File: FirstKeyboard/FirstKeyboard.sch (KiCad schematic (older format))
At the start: 2 parts

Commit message: A little more done
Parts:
- added C? (x2): 22pF, symbol Device:C_Small
- added C?: 100n, symbol Device:C_Small
- added C?: 1uF, symbol Device:C_Small
- added R? (x2): 10k, symbol Device:R_Small
- added SW?: SW_Push, symbol Switch:SW_Push
- added Y?: 16MHz, symbol Device:Crystal_Small
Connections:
- net +5V: now also R?.2
- net GND: now also C?.1, C?.1, C?.2, R?.1, SW?.1
- net RST: now reaches U?.13 (~RESET)
- net RST: now also C?.2, R?.1, SW?.2
- net at U?.16 (XTAL2): now also C?.2, Y?.1
- net at U?.17 (XTAL1): now also C?.1, Y?.2
- net at U?.33 (~HWB~/PE2): now also R?.2
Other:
- moved on the sheet: C?, U?

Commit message: Morning Updates Dec9
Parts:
- removed C?: 1uF, symbol Device:C_Small
- added C? (x2): 100n, symbol Device:C_Small
- added C?: 1uF, symbol Device:C_Small
- added C?: 10uF, symbol Device:C_Small
- added J?: USB_B_Mini, symbol Connector:USB_B_Mini
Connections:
- net +5V: now also C?.1, C?.1, C?.1, C?.1
- net GND: now also C?.2, C?.2, C?.2, C?.2
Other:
- moved on the sheet: C?, R?, SW?, U?, Y?

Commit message: added gitignore and other files
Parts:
- added D1, D2, D3, D4: D_Small, symbol Device:D_Small
- added R2, R3: 22R, symbol Device:R_Small
- added SW1, SW2, SW3, SW4: MXSwitch, symbol acheronSymbols:MXSwitch
- gave numbers to parts that had none: 14
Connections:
- net +5V: now also J1.1 (VBUS)
- net GND: now also J1.5 (GND)
- net at U1.3 (D-): now also R3.2
- net at U1.4 (D+): now also R2.1
- net at J1.2 (D-): now also R3.1
- net at J1.3 (D+): now also R2.2
- new net: D1.2 (A), SW1.2 (Row)
- new net: D3.2 (A), SW3.2 (Row)
- new net: D4.2 (A), SW4.2 (Row)
- new net: D2.2 (A), SW2.2 (Row)
- new net Col1: D1.1 (K), D3.1 (K)
- new net Col2: D2.1 (K), D4.1 (K)
- new net Row1: SW1.1 (Col), SW2.1 (Col)
- new net Row2: SW3.1 (Col), SW4.1 (Col)
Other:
- moved on the sheet: C1, C2, C3, C4, C5, C6, C7, C8, J1, R1, R4, SWP1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

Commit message: Last update of the day
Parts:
- C1, C2, C3, C4, C5, C6, C7, C8: footprint (none) -> Capacitor_SMD:C_0805_2012Metric_Pad1.15x1.40mm_HandSolder
- D1, D2, D3, D4: footprint (none) -> Diode_SMD:D_SOD-123
- J1: footprint (none) -> acheron_Connectors:USB_MiniB_XM7D-0512
- R1, R2, R3, R4: footprint (none) -> Resistor_SMD:R_1206_3216Metric_Pad1.42x1.75mm_HandSolder
- SW1, SW2, SW3, SW4: footprint (none) -> acheron_MX:MX100
- SWP1: footprint (none) -> acheron_Hardware:smdPushBtn
- Y1: footprint (none) -> Crystal:Crystal_SMD_5032-2Pin_5.0x3.2mm_HandSoldering
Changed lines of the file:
@@
 F 0 "SW1" H 7000 3000 50  0000 L CNN
 F 1 "MXSwitch" H 6950 2925 39  0000 L CNN
-F 2 "" H 7075 2925 50  0001 C CNN
+F 2 "acheron_MX:MX100" H 7075 2925 50  0001 C CNN
 F 3 "" H 7075 2925 50  0001 C CNN
 	1    7075 2925
@@
 F 0 "D1" V 7029 2543 50  0000 L CNN
 F 1 "D_Small" V 7120 2543 50  0000 L CNN
-F 2 "" V 7075 2475 50  0001 C CNN
+F 2 "Diode_SMD:D_SOD-123" V 7075 2475 50  0001 C CNN
 F 3 "~" V 7075 2475 50  0001 C CNN
 	1    7075 2475
@@
 F 0 "SW3" H 7925 3000 50  0000 L CNN
 F 1 "MXSwitch" H 7875 2925 39  0000 L CNN
-F 2 "" H 8000 2925 50  0001 C CNN
+F 2 "acheron_MX:MX100" H 8000 2925 50  0001 C CNN
 F 3 "" H 8000 2925 50  0001 C CNN
 	1    8000 2925
@@
 F 0 "D3" V 7954 2543 50  0000 L CNN
 F 1 "D_Small" V 8045 2543 50  0000 L CNN
-F 2 "" V 8000 2475 50  0001 C CNN
+F 2 "Diode_SMD:D_SOD-123" V 8000 2475 50  0001 C CNN
 F 3 "~" V 8000 2475 50  0001 C CNN
 	1    8000 2475
@@
 F 0 "SW4" H 7925 4275 50  0000 L CNN
 F 1 "MXSwitch" H 7875 4200 39  0000 L CNN
-F 2 "" H 8000 4200 50  0001 C CNN
+F 2 "acheron_MX:MX100" H 8000 4200 50  0001 C CNN
 F 3 "" H 8000 4200 50  0001 C CNN
 	1    8000 4200
@@
 F 0 "D4" V 7954 3818 50  0000 L CNN
 F 1 "D_Small" V 8045 3818 50  0000 L CNN
-F 2 "" V 8000 3750 50  0001 C CNN
+F 2 "Diode_SMD:D_SOD-123" V 8000 3750 50  0001 C CNN
 F 3 "~" V 8000 3750 50  0001 C CNN
 	1    8000 3750
@@
 F 0 "SW2" H 7000 4275 50  0000 L CNN
 F 1 "MXSwitch" H 6950 4200 39  0000 L CNN
-F 2 "" H 7075 4200 50  0001 C CNN
+F 2 "acheron_MX:MX100" H 7075 4200 50  0001 C CNN
 F 3 "" H 7075 4200 50  0001 C CNN
 	1    7075 4200
@@
 F 0 "D2" V 7029 3818 50  0000 L CNN
 F 1 "D_Small" V 7120 3818 50  0000 L CNN
-F 2 "" V 7075 3750 50  0001 C CNN
+F 2 "Diode_SMD:D_SOD-123" V 7075 3750 50  0001 C CNN
 F 3 "~" V 7075 3750 50  0001 C CNN
 	1    7075 3750
@@
 F 0 "R3" V 2604 5000 50  0000 C CNN
 F 1 "22R" V 2695 5000 50  0000 C CNN
-F 2 "" H 2800 5000 50  0001 C CNN
+F 2 "Resistor_SMD:R_1206_3216Metric_Pad1.42x1.75mm_HandSolder" H 2800 5000 50  0001 C CNN
 F 3 "~" H 2800 5000 50  0001 C CNN
 	1    2800 5000
@@
 F 0 "R2" V 2604 4900 50  0000 C CNN
 F 1 "22R" V 2695 4900 50  0000 C CNN
-F 2 "" H 2800 4900 50  0001 C CNN
+F 2 "Resistor_SMD:R_1206_3216Metric_Pad1.42x1.75mm_HandSolder" H 2800 4900 50  0001 C CNN
 F 3 "~" H 2800 4900 50  0001 C CNN
 	1    2800 4900
@@
 F 0 "J1" H 2150 5375 50  0000 C CNN
 F 1 "USB_B_Mini" H 2150 5275 50  0000 C CNN
-F 2 "" H 2300 4850 50  0001 C CNN
+F 2 "acheron_Connectors:USB_MiniB_XM7D-0512" H 2300 4850 50  0001 C CNN
 F 3 "~" H 2300 4850 50  0001 C CNN
 	1    2150 4900
@@
 F 0 "C5" V 3825 2575 50  0000 C CNN
 F 1 "10uF" V 3725 2575 50  0000 C CNN
-F 2 "" H 3625 2575 50  0001 C CNN
+F 2 "Capacitor_SMD:C_0805_2012Metric_Pad1.15x1.40mm_HandSolder" H 3625 2575 50  0001 C CNN
 F 3 "~" H 3625 2575 50  0001 C CNN
 	1    3625 2575
@@
 F 0 "C6" V 4125 2575 50  0000 C CNN
 F 1 "1uF" V 4025 2575 50  0000 C CNN
-F 2 "" H 3925 2575 50  0001 C CNN
+F 2 "Capacitor_SMD:C_0805_2012Metric_Pad1.15x1.40mm_HandSolder" H 3925 2575 50  0001 C CNN
 F 3 "~" H 3925 2575 50  0001 C CNN
 	1    3925 2575
@@
 F 0 "C7" V 4425 2575 50  0000 C CNN
 F 1 "100n" V 4325 2575 50  0000 C CNN
-F 2 "" H 4225 2575 50  0001 C CNN
+F 2 "Capacitor_SMD:C_0805_2012Metric_Pad1.15x1.40mm_HandSolder" H 4225 2575 50  0001 C CNN
 F 3 "~" H 4225 2575 50  0001 C CNN
 	1    4225 2575
@@
 F 0 "C8" V 4725 2575 50  0000 C CNN
 F 1 "100n" V 4625 2575 50  0000 C CNN
-F 2 "" H 4525 2575 50  0001 C CNN
+F 2 "Capacitor_SMD:C_0805_2012Metric_Pad1.15x1.40mm_HandSolder" H 4525 2575 50  0001 C CNN
 F 3 "~" H 4525 2575 50  0001 C CNN
 	1    4525 2575
@@
 F 0 "R1" H 2716 2854 50  0000 R CNN
 F 1 "10k" H 2716 2945 50  0000 R CNN
-F 2 "" H 2775 2900 50  0001 C CNN
+F 2 "Resistor_SMD:R_1206_3216Metric_Pad1.42x1.75mm_HandSolder" H 2775 2900 50  0001 C CNN
 F 3 "~" H 2775 2900 50  0001 C CNN
 	1    2775 2900
@@
 F 0 "SWP1" H 2700 3550 50  0000 R CNN
 F 1 "SW_Push" H 2725 3450 50  0000 R CNN
-F 2 "" H 2575 3400 50  0001 C CNN
+F 2 "acheron_Hardware:smdPushBtn" H 2575 3400 50  0001 C CNN
 F 3 "~" H 2575 3400 50  0001 C CNN
 	1    2575 3200
@@
 F 0 "C1" H 3025 3100 50  0000 R CNN
 F 1 "100n" H 3075 3300 50  0000 R CNN
-F 2 "" H 3075 3200 50  0001 C CNN
+F 2 "Capacitor_SMD:C_0805_2012Metric_Pad1.15x1.40mm_HandSolder" H 3075 3200 50  0001 C CNN
 F 3 "~" H 3075 3200 50  0001 C CNN
 	1    3075 3200
@@
 F 0 "R4" V 4729 6000 50  0000 C CNN
 F 1 "10k" V 4820 6000 50  0000 C CNN
-F 2 "" H 4925 6000 50  0001 C CNN
+F 2 "Resistor_SMD:R_1206_3216Metric_Pad1.42x1.75mm_HandSolder" H 4925 6000 50  0001 C CNN
 F 3 "~" H 4925 6000 50  0001 C CNN
 	1    4925 6000
@@
 F 0 "C3" V 2896 4300 50  0000 C CNN
 F 1 "22pF" V 2987 4300 50  0000 C CNN
-F 2 "" H 3125 4300 50  0001 C CNN
+F 2 "Capacitor_SMD:C_0805_2012Metric_Pad1.15x1.40mm_HandSolder" H 3125 4300 50  0001 C CNN
 F 3 "~" H 3125 4300 50  0001 C CNN
 	1    3125 4300
@@
 F 0 "C2" V 2975 4250 50  0000 C CNN
 F 1 "22pF" V 2987 4100 50  0000 C CNN
-F 2 "" H 3125 4100 50  0001 C CNN
+F 2 "Capacitor_SMD:C_0805_2012Metric_Pad1.15x1.40mm_HandSolder" H 3125 4100 50  0001 C CNN
 F 3 "~" H 3125 4100 50  0001 C CNN
 	1    3125 4100
@@
 F 0 "Y1" V 3225 4250 50  0000 R CNN
 F 1 "16MHz" V 3125 4300 50  0000 R CNN
-F 2 "" H 3375 4200 50  0001 C CNN
+F 2 "Crystal:Crystal_SMD_5032-2Pin_5.0x3.2mm_HandSoldering" H 3375 4200 50  0001 C CNN
 F 3 "~" H 3375 4200 50  0001 C CNN
 	1    3375 4200
@@
 F 0 "C4" V 3575 5200 50  0000 C CNN
 F 1 "1uF" V 3675 5200 50  0000 C CNN
-F 2 "" H 3425 5200 50  0001 C CNN
+F 2 "Capacitor_SMD:C_0805_2012Metric_Pad1.15x1.40mm_HandSolder" H 3425 5200 50  0001 C CNN
 F 3 "~" H 3425 5200 50  0001 C CNN
 	1    3425 5200

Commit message: Dec10 Update, Starting full board
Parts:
- added D? (x84): 1N4148W, Diode_SMD:D_SOD-123, symbol Device:D_Small
- added R5: 330, Resistor_SMD:R_1206_3216Metric_Pad1.42x1.75mm_HandSolder, symbol Device:R_Small
- added SW?: F2, acheron_MX:MX100, symbol acheronSymbols:MXSwitch
- added SW?: F3, acheron_MX:MX100, symbol acheronSymbols:MXSwitch
- added SW?: F4, acheron_MX:MX100, symbol acheronSymbols:MXSwitch
- added SW?: F5, acheron_MX:MX100, symbol acheronSymbols:MXSwitch
- added SW?: F6, acheron_MX:MX100, symbol acheronSymbols:MXSwitch
- added SW?: F7, acheron_MX:MX100, symbol acheronSymbols:MXSwitch
- added SW?: F8, acheron_MX:MX100, symbol acheronSymbols:MXSwitch
- added SW?: F9, acheron_MX:MX100, symbol acheronSymbols:MXSwitch
- added SW?: Ins, acheron_MX:MX100, symbol acheronSymbols:MXSwitch
- added SW?: End, acheron_MX:MX100, symbol acheronSymbols:MXSwitch
- added SW?: Home, acheron_MX:MX100, symbol acheronSymbols:MXSwitch
- added SW?: F12, acheron_MX:MX100, symbol acheronSymbols:MXSwitch
- added SW?: F11, acheron_MX:MX100, symbol acheronSymbols:MXSwitch
- added SW?: F10, acheron_MX:MX100, symbol acheronSymbols:MXSwitch
- added SW?: Two, acheron_MX:MX100, symbol acheronSymbols:MXSwitch
- added SW?: Nine, acheron_MX:MX100, symbol acheronSymbols:MXSwitch
- added SW?: Eight, acheron_MX:MX100, symbol acheronSymbols:MXSwitch
- added SW?: Seven, acheron_MX:MX100, symbol acheronSymbols:MXSwitch
- added SW?: Six, acheron_MX:MX100, symbol acheronSymbols:MXSwitch
- added SW?: Five, acheron_MX:MX100, symbol acheronSymbols:MXSwitch
- added SW?: Four, acheron_MX:MX100, symbol acheronSymbols:MXSwitch
- added SW?: Three, acheron_MX:MX100, symbol acheronSymbols:MXSwitch
- added SW?: Delete, acheron_MX:MX100, symbol acheronSymbols:MXSwitch
- added SW?: BkSpc, acheron_MX:MX100, symbol acheronSymbols:MXSwitch
- added SW?: Plus, acheron_MX:MX100, symbol acheronSymbols:MXSwitch
- added SW?: Minus, acheron_MX:MX100, symbol acheronSymbols:MXSwitch
- added SW?: Zero, acheron_MX:MX100, symbol acheronSymbols:MXSwitch
- added SW?: Tab, acheron_MX:MX100, symbol acheronSymbols:MXSwitch
- added SW?: Q, acheron_MX:MX100, symbol acheronSymbols:MXSwitch
- added SW?: CapsL, acheron_MX:MX100, symbol acheronSymbols:MXSwitch
- added SW?: A, acheron_MX:MX100, symbol acheronSymbols:MXSwitch
- added SW?: Shift, acheron_MX:MX100, symbol acheronSymbols:MXSwitch
- added SW?: Ctrl, acheron_MX:MX100, symbol acheronSymbols:MXSwitch
- added SW?: Super, acheron_MX:MX100, symbol acheronSymbols:MXSwitch
- added SW?: W, acheron_MX:MX100, symbol acheronSymbols:MXSwitch
- added SW?: O, acheron_MX:MX100, symbol acheronSymbols:MXSwitch
- added SW?: I, acheron_MX:MX100, symbol acheronSymbols:MXSwitch
- added SW?: U, acheron_MX:MX100, symbol acheronSymbols:MXSwitch
- added SW?: Y, acheron_MX:MX100, symbol acheronSymbols:MXSwitch
- added SW?: T, acheron_MX:MX100, symbol acheronSymbols:MXSwitch
- added SW?: R, acheron_MX:MX100, symbol acheronSymbols:MXSwitch
- added SW?: E, acheron_MX:MX100, symbol acheronSymbols:MXSwitch
- added SW?: PgUp, acheron_MX:MX100, symbol acheronSymbols:MXSwitch
- added SW?: \\, acheron_MX:MX100, symbol acheronSymbols:MXSwitch
- added SW?: ], acheron_MX:MX100, symbol acheronSymbols:MXSwitch
- added SW?: [, acheron_MX:MX100, symbol acheronSymbols:MXSwitch
- added SW?: P, acheron_MX:MX100, symbol acheronSymbols:MXSwitch
- added SW?: S, acheron_MX:MX100, symbol acheronSymbols:MXSwitch
- added SW?: L, acheron_MX:MX100, symbol acheronSymbols:MXSwitch
- added SW?: K, acheron_MX:MX100, symbol acheronSymbols:MXSwitch
- added SW?: J, acheron_MX:MX100, symbol acheronSymbols:MXSwitch
- added SW?: H, acheron_MX:MX100, symbol acheronSymbols:MXSwitch
- added SW?: G, acheron_MX:MX100, symbol acheronSymbols:MXSwitch
- added SW?: F, acheron_MX:MX100, symbol acheronSymbols:MXSwitch
- added SW?: D, acheron_MX:MX100, symbol acheronSymbols:MXSwitch
- added SW?: PgDn, acheron_MX:MX100, symbol acheronSymbols:MXSwitch
- added SW? (x8): MXSwitch, acheron_MX:MX100, symbol acheronSymbols:MXSwitch
- added SW?: Quote, acheron_MX:MX100, symbol acheronSymbols:MXSwitch
- added SW?: Colon, acheron_MX:MX100, symbol acheronSymbols:MXSwitch
- added SW?: X, acheron_MX:MX100, symbol acheronSymbols:MXSwitch
- added SW?: RCarrot, acheron_MX:MX100, symbol acheronSymbols:MXSwitch
- added SW?: LCarrot, acheron_MX:MX100, symbol acheronSymbols:MXSwitch
- added SW?: M, acheron_MX:MX100, symbol acheronSymbols:MXSwitch
- added SW?: N, acheron_MX:MX100, symbol acheronSymbols:MXSwitch
- added SW?: B, acheron_MX:MX100, symbol acheronSymbols:MXSwitch
- added SW?: V, acheron_MX:MX100, symbol acheronSymbols:MXSwitch
- added SW?: C, acheron_MX:MX100, symbol acheronSymbols:MXSwitch
- added SW?: Up, acheron_MX:MX100, symbol acheronSymbols:MXSwitch
- added SW?: Quest, acheron_MX:MX100, symbol acheronSymbols:MXSwitch
- added SW? (x2): Alt, acheron_MX:MX100, symbol acheronSymbols:MXSwitch
- added SW?: Space, acheron_MX:MX100, symbol acheronSymbols:MXSwitch
- added SW?: Right, acheron_MX:MX100, symbol acheronSymbols:MXSwitch
- added SW?: Down, acheron_MX:MX100, symbol acheronSymbols:MXSwitch
- added SW?: Left, acheron_MX:MX100, symbol acheronSymbols:MXSwitch
- added SW?: Fn, acheron_MX:MX100, symbol acheronSymbols:MXSwitch
- added SW?: Z, acheron_MX:MX100, symbol acheronSymbols:MXSwitch
- D1, D2, D3, D4: value D_Small -> 1N4148W
- R4: value 10k -> 1k
- SW1: value MXSwitch -> Esc
- SW2: value MXSwitch -> Tilde
- SW3: value MXSwitch -> F1
- SW4: value MXSwitch -> One
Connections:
- net Col1: now also SW1.1 (Col), SW2.1 (Col), SW?.1 (Col), SW?.1 (Col), SW?.1 (Col), SW?.1 (Col); no longer D1.1 (K), D3.1 (K)
- net Col2: now also SW3.1 (Col), SW4.1 (Col), SW?.1 (Col), SW?.1 (Col), SW?.1 (Col), SW?.1 (Col); no longer D2.1 (K), D4.1 (K)
- net GND: now also R5.2; no longer C1.1, SWP1.1
- net Row1: now also D1.1 (K), D3.1 (K), D?.1 (K), D?.1 (K), D?.1 (K), D?.1 (K), D?.1 (K), D?.1 (K), D?.1 (K), D?.1 (K), D?.1 (K), D?.1 (K), D?.1 (K), D?.1 (K), D?.1 (K), D?.1 (K); no longer SW1.1 (Col), SW2.1 (Col)
- net Row2: now also D2.1 (K), D4.1 (K), D?.1 (K), D?.1 (K), D?.1 (K), D?.1 (K), D?.1 (K), D?.1 (K), D?.1 (K), D?.1 (K), D?.1 (K), D?.1 (K), D?.1 (K), D?.1 (K), D?.1 (K); no longer SW3.1 (Col), SW4.1 (Col)
- new net: C1.1, R5.1, SWP1.1
- new net: D?.2 (A), SW?.2 (Row) (x84)
- new net Col10: SW?.1 (Col), SW?.1 (Col), SW?.1 (Col), SW?.1 (Col), SW?.1 (Col), SW?.1 (Col)
- new net Col11: SW?.1 (Col), SW?.1 (Col), SW?.1 (Col), SW?.1 (Col), SW?.1 (Col), SW?.1 (Col)
- new net Col12: SW?.1 (Col), SW?.1 (Col), SW?.1 (Col), SW?.1 (Col), SW?.1 (Col)
- new net Col13: SW?.1 (Col), SW?.1 (Col), SW?.1 (Col), SW?.1 (Col), SW?.1 (Col), SW?.1 (Col)
- new net Col14: SW?.1 (Col), SW?.1 (Col), SW?.1 (Col), SW?.1 (Col), SW?.1 (Col), SW?.1 (Col)
- new net Col15: SW?.1 (Col), SW?.1 (Col), SW?.1 (Col), SW?.1 (Col), SW?.1 (Col), SW?.1 (Col)
- new net Col16: SW?.1 (Col)
- new net Col3: SW?.1 (Col), SW?.1 (Col), SW?.1 (Col), SW?.1 (Col), SW?.1 (Col), SW?.1 (Col)
- new net Col4: SW?.1 (Col), SW?.1 (Col), SW?.1 (Col), SW?.1 (Col), SW?.1 (Col)
- new net Col5: SW?.1 (Col), SW?.1 (Col), SW?.1 (Col), SW?.1 (Col), SW?.1 (Col)
- new net Col6: SW?.1 (Col), SW?.1 (Col), SW?.1 (Col), SW?.1 (Col), SW?.1 (Col), SW?.1 (Col)
- new net Col7: SW?.1 (Col), SW?.1 (Col), SW?.1 (Col), SW?.1 (Col), SW?.1 (Col), SW?.1 (Col)
- new net Col8: SW?.1 (Col), SW?.1 (Col), SW?.1 (Col), SW?.1 (Col), SW?.1 (Col), SW?.1 (Col)
- new net Col9: SW?.1 (Col), SW?.1 (Col), SW?.1 (Col), SW?.1 (Col), SW?.1 (Col), SW?.1 (Col)
- new net Row3: D?.1 (K), D?.1 (K), D?.1 (K), D?.1 (K), D?.1 (K), D?.1 (K), D?.1 (K), D?.1 (K), D?.1 (K), D?.1 (K), D?.1 (K), D?.1 (K), D?.1 (K), D?.1 (K), D?.1 (K)
- new net Row4: D?.1 (K), D?.1 (K), D?.1 (K), D?.1 (K), D?.1 (K), D?.1 (K), D?.1 (K), D?.1 (K), D?.1 (K), D?.1 (K), D?.1 (K), D?.1 (K), D?.1 (K), D?.1 (K), D?.1 (K)
- new net Row5: D?.1 (K), D?.1 (K), D?.1 (K), D?.1 (K), D?.1 (K), D?.1 (K), D?.1 (K), D?.1 (K), D?.1 (K), D?.1 (K), D?.1 (K), D?.1 (K), D?.1 (K), D?.1 (K), D?.1 (K)
- new net Row6: D?.1 (K), D?.1 (K), D?.1 (K), D?.1 (K), D?.1 (K), D?.1 (K), D?.1 (K), D?.1 (K), D?.1 (K), D?.1 (K), D?.1 (K), D?.1 (K)
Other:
- moved on the sheet: C1, C2, C3, C4, C5, C6, C7, C8, D1, D2, D3, D4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

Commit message: Finished Schematic?
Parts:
- removed D? (x6): 1N4148W, Diode_SMD:D_SOD-123, symbol Device:D_Small
- removed SW? (x4): MXSwitch, acheron_MX:MX100, symbol acheronSymbols:MXSwitch
- removed SW?: Fn, acheron_MX:MX100, symbol acheronSymbols:MXSwitch
- removed SW?: Z, acheron_MX:MX100, symbol acheronSymbols:MXSwitch
- SW16: renamed from SW?; value X -> Z
- SW22: renamed from SW?; value C -> X
- SW27: renamed from SW?; value V -> C
- SW32: renamed from SW?; value B -> V
- SW37: renamed from SW?; value N -> B
- SW43: renamed from SW?; value M -> N
- SW48: renamed from SW?; value LCarrot -> M
- SW53: renamed from SW?; value RCarrot -> <
- SW58: renamed from SW?; value Quest -> >
- SW59: renamed from SW?; value MXSwitch -> Alt
- SW64: renamed from SW?; value MXSwitch -> ?
- SW65: renamed from SW?; value Alt -> Fn
- SW69: renamed from SW?; value MXSwitch -> Shift
- SW74: renamed from SW?; value MXSwitch -> Enter
- gave numbers to parts that had none: 142
- renumbered C4 to C1, C3 to C2, C2 to C3, C1 to C4, D3 to D7, D4 to D8, R4 to R1, R3 to R2, R2 to R3, R5 to R4, R1 to R5, SW3 to SW7, SW4 to SW8
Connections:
- net Col10: no longer SW65.1 (Col)
- net Col11: now also SW59.1 (Col)
- net Col12: now also SW65.1 (Col)
- net Col13: no longer SW74.1 (Col)
- net Col14: now also SW74.1 (Col), SW75.1 (Col)
- net Col15: no longer SW75.1 (Col)
- net Col6: no longer SW38.1 (Col)
- net Col7: now also SW38.1 (Col)
- net Col9: no longer SW59.1 (Col)
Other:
- moved on the sheet: D38, D59, D65, D74, D75, SW38, SW59, SW65, SW74, SW75

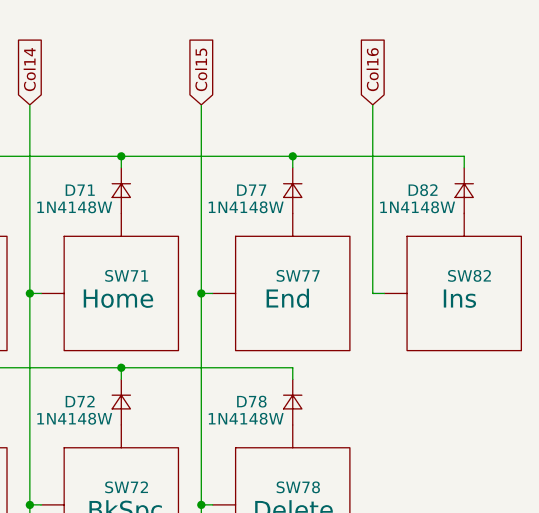
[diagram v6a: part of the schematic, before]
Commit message: Removed the "INS" key
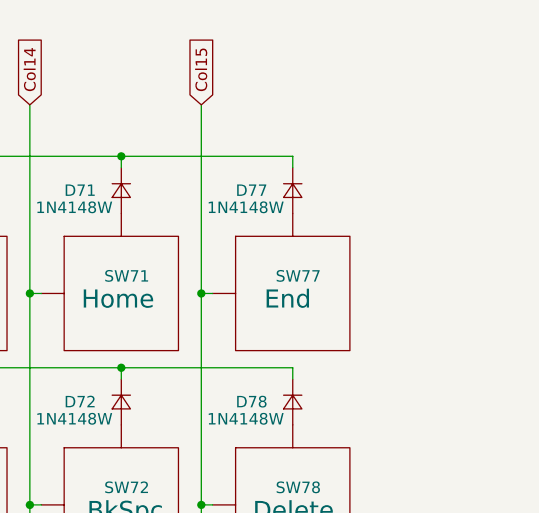
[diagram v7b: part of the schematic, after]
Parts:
- removed D82: 1N4148W, Diode_SMD:D_SOD-123, symbol Device:D_Small
- removed SW82: Ins, acheron_MX:MX100, symbol acheronSymbols:MXSwitch
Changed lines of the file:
@@
 	8150 1475 8900 1475
 Wire Wire Line
-	13400 1525 13400 1475
-Wire Wire Line
 	10400 1525 10400 1475
-$Comp
-L Device:D_Small D82
-U 1 1 5E0CFDC0
-P 13400 1625
-F 0 "D82" V 13400 1375 50  0000 L CNN
-F 1 "1N4148W" V 13475 1250 50  0000 L CNN
-F 2 "Diode_SMD:D_SOD-123" V 13400 1625 50  0001 C CNN
-F 3 "~" V 13400 1625 50  0001 C CNN
-	1    13400 1625
-	0    1    1    0
-$EndComp
-$Comp
-L acheronSymbols:MXSwitch SW82
-U 1 1 5E0CFDC6
-P 13400 2075
-F 0 "SW82" H 13325 2150 50  0000 L CNN
-F 1 "Ins" H 13300 2050 79  0000 L CNN
-F 2 "acheron_MX:MX100" H 13400 2075 50  0001 C CNN
-F 3 "" H 13400 2075 50  0001 C CNN
-	1    13400 2075
-	1    0    0    -1
-$EndComp
-$Comp
-L acheronSymbols:MXSwitch SW77
-U 1 1 5E0CFDCC
-P 12650 2075
-F 0 "SW77" H 12575 2150 50  0000 L CNN
-F 1 "End" H 12525 2050 79  0000 L CNN
-F 2 "acheron_MX:MX100" H 12650 2075 50  0001 C CNN
-F 3 "" H 12650 2075 50  0001 C CNN
-	1    12650 2075
-	1    0    0    -1
-$EndComp
 $Comp
 L Device:D_Small D77
@@
 Wire Wire Line
 	11900 1475 12650 1475
-Connection ~ 12650 1475
-Wire Wire Line
-	12650 1475 13400 1475
 Connection ~ 8900 1475
 Text GLabel 1550 3325 0    50   Input ~ 0
@@
 $EndComp
 $Comp
-L acheronSymbols:MXSwitch SW78
-U 1 1 5E0ED070
-P 12650 3000
-F 0 "SW78" H 12575 3075 50  0000 L CNN
-F 1 "Delete" H 12475 2975 79  0000 L CNN
-F 2 "acheron_MX:MX100" H 12650 3000 50  0001 C CNN
-F 3 "" H 12650 3000 50  0001 C CNN
-	1    12650 3000
-	1    0    0    -1
-$EndComp
-$Comp
 L Device:D_Small D72
 U 1 1 5E0ED085
@@
 Wire Wire Line
 	12250 3000 12250 2075
-Wire Wire Line
-	13050 2075 13000 2075
-Wire Wire Line
-	13000 2075 13000 1250
 Text GLabel 3250 1250 1    50   Input ~ 0
 Col3
@@
 Text GLabel 12250 1250 1    50   Input ~ 0
 Col15
-Text GLabel 13000 1250 1    50   Input ~ 0
-Col16
 $Comp
 L acheronSymbols:MXSwitch SW63
@@
 Wire Wire Line
 	10750 3925 10750 5775
+$Comp
+L acheronSymbols:MXSwitch SW78
+U 1 1 5E0ED070
+P 12650 3000
+F 0 "SW78" H 12575 3075 50  0000 L CNN
+F 1 "Delete" H 12475 2975 79  0000 L CNN
+F 2 "acheron_MX:MX100" H 12650 3000 50  0001 C CNN
+F 3 "" H 12650 3000 50  0001 C CNN
+	1    12650 3000
+	1    0    0    -1
+$EndComp
+$Comp
+L acheronSymbols:MXSwitch SW77
+U 1 1 5E0CFDCC
+P 12650 2075
+F 0 "SW77" H 12575 2150 50  0000 L CNN
+F 1 "End" H 12525 2050 79  0000 L CNN
+F 2 "acheron_MX:MX100" H 12650 2075 50  0001 C CNN
+F 3 "" H 12650 2075 50  0001 C CNN
+	1    12650 2075
+	1    0    0    -1
+$EndComp
 $EndSCHEMATC

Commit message: Small update to Aly keys
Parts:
- SW17: value Alt -> LAlt
- SW59: value Alt -> RAlt
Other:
- moved on the sheet: C1, C2, C3, C4, C5, C6, C7, C8, D1, D10, D11, D12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
